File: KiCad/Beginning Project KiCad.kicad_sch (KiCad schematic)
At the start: 3 parts

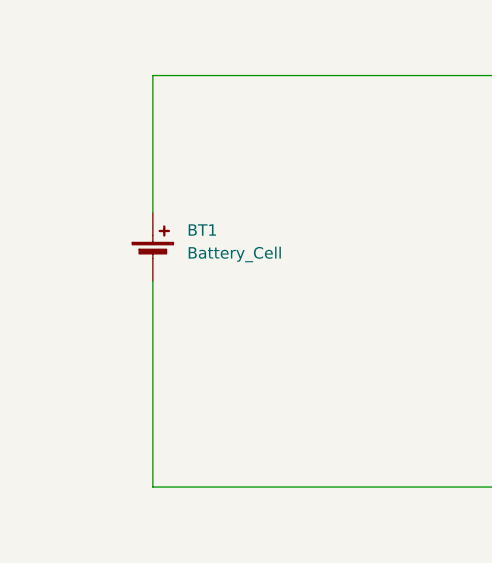
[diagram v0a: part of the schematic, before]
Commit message: Created first board
This tutorial covers Part 3 of the KiCad part 3 tutorial which gives me a chance to play around with the setting of copper zones, Design Rule Checking, routing tracks, and placing symbols from the previous schematic.
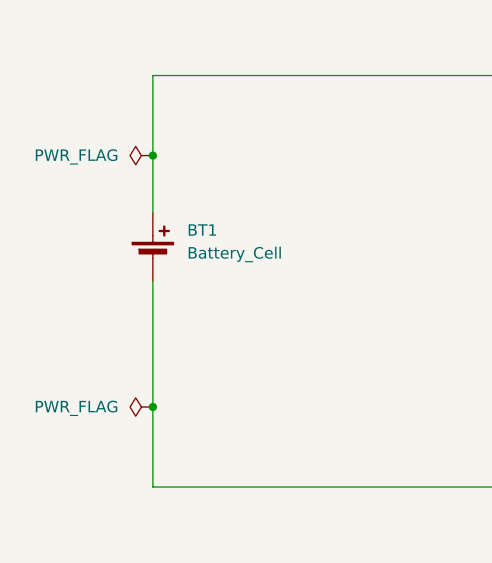
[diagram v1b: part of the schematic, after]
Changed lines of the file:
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@@
+	)
+	(junction
+		(at 71.12 83.82)
+		(diameter 0)
+		(color 0 0 0 0)
 	)
 	(junction
@@
 		(color 0 0 0 0)
 	)
+	(junction
+		(at 71.12 111.76)
+		(diameter 0)
+		(color 0 0 0 0)
+	)
+	(wire
+		(pts
+			(xy 71.12 83.82) (xy 71.12 74.93)
+		)
+		(stroke
+			(width 0)
+			(type default)
+		)
+	)
 	(wire
 		(pts
@@
 	(wire
 		(pts
-			(xy 71.12 120.65) (xy 71.12 97.79)
+			(xy 71.12 120.65) (xy 71.12 111.76)
 		)
 		(stroke
@@
 	(wire
 		(pts
-			(xy 71.12 90.17) (xy 71.12 74.93)
+			(xy 71.12 90.17) (xy 71.12 83.82)
 		)
 		(stroke
@@
 		(pts
 			(xy 176.53 83.82) (xy 176.53 93.98)
+		)
+		(stroke
+			(width 0)
+			(type default)
+		)
+	)
+	(wire
+		(pts
+			(xy 71.12 111.76) (xy 71.12 97.79)
 		)
 		(stroke
@@
 	)
 	(symbol
+		(lib_id "power:PWR_FLAG")
+		(at 71.12 111.76 90)
+		(unit 1)
+		(exclude_from_sim no)
+		(in_bom yes)
+		(on_board yes)
+		(dnp no)
+		(fields_autoplaced yes)
+		(property "Reference" "#FLG01"
+			(at 69.215 111.76 0)
+			(effects
+				(font
+					(size 1.27 1.27)
+				)
+				(hide yes)
+			)
+		)
+		(property "Value" "PWR_FLAG"
+			(at 67.31 111.7599 90)
+			(effects
+				(font
+					(size 1.27 1.27)
+				)
+				(justify left)
+			)
+		)
+		(property "Footprint" ""
+			(at 71.12 111.76 0)
+			(effects
+				(font
+					(size 1.27 1.27)
+				)
+				(hide yes)
+			)
+		)
+		(property "Datasheet" "~"
+			(at 71.12 111.76 0)
+			(effects
+				(font
+					(size 1.27 1.27)
+				)
+				(hide yes)
+			)
+		)
+		(property "Description" "Special symbol for telling ERC where power comes from"
+			(at 71.12 111.76 0)
+			(effects
+				(font
+					(size 1.27 1.27)
+				)
+				(hide yes)
+			)
+		)
+		(pin "1"
+		)
+		(instances
+			(project ""
+				(path "/84d97a86-4222-443f-9aa6-7ff5d448ba14"
+					(reference "#FLG01")
+					(unit 1)
+				)
+			)
+		)
+	)
+	(symbol
 		(lib_id "Device:R_Small_US")
 		(at 176.53 81.28 0)
@@
 					(unit 1)
 				)
+			)
+		)
+	)
+	(symbol
+		(lib_id "power:PWR_FLAG")
+		(at 71.12 83.82 90)
+		(unit 1)
+		(exclude_from_sim no)
+		(in_bom yes)
+		(on_board yes)
+		(dnp no)
+		(fields_autoplaced yes)
+		(property "Reference" "#FLG02"
+			(at 69.215 83.82 0)
+			(effects
+				(font
+					(size 1.27 1.27)
+				)
+				(hide yes)
+			)
+		)
+		(property "Value" "PWR_FLAG"
+			(at 67.31 83.8199 90)
+			(effects
+				(font
+					(size 1.27 1.27)
+				)
+				(justify left)
+			)
+		)
+		(property "Footprint" ""
+			(at 71.12 83.82 0)
+			(effects
+				(font
+					(size 1.27 1.27)
+				)
+				(hide yes)
+			)
+		)
+		(property "Datasheet" "~"
+			(at 71.12 83.82 0)
+			(effects
+				(font
+					(size 1.27 1.27)
+				)
+				(hide yes)
+			)
+		)
+		(property "Description" "Special symbol for telling ERC where power comes from"
+			(at 71.12 83.82 0)
+			(effects
+				(font
+					(size 1.27 1.27)
+				)
+				(hide yes)
+			)
+		)
+		(pin "1"
+		)
+		(instances
+			(project "Beginning Project KiCad"
+				(path "/84d97a86-4222-443f-9aa6-7ff5d448ba14"
+					(reference "#FLG02")
+					(unit 1)
+				)
